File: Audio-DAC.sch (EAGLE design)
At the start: 200 parts, among them CON1 USB-5075BR-04-WH, CON2 VOL_CON, CON3 SWD_CON, IC1 3.3V 200mA, IC10 15V, IC11 -15V, IC12 3.3V, IC13 LPC1114FDH28, IC14 10V, IC15 5V, IC16 5V, IC17 3.3V, IC18 TC7WH74FU, IC19 AK4495EQ, IC2 AT32UC3A3256, IC20 TC7WU04FU, IC21 10V, IC22 -10V, IC23 OP275, IC3 SI8420, IC4 SI8420, IC5 SI8420, IC6 SI8420, IC9 7805, Q1 NPN2SC3422, Q2 PNP2SA1359, Q3 NPN2SC3422, Q4 PNP2SA1359, Q5 NPN2SC3325, Q6 NPN2SC3325, SW1 EA2, SW2 EA2, X1 12MHz, X2 24.576MHz, X3 22.5792MHz

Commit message: 微調整
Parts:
- added FB4: FB-1608, my_rcl:FB-1608
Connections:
- new net N$14: C43.1, C44.1, FB4.2, X2.VCC, X3.VCC
- new net UART_RX: IC2G$2.PX04
- new net UART_TX: IC2G$2.PX05
- net DAC_AVDD: now also FB4.1; no longer C43.1, C44.1, X2.VCC, X3.VCC
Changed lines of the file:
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@@
 <part name="SUPPLY133" library="my_supply" deviceset="DGND" device=""/>
 <part name="SUPPLY116" library="my_supply" deviceset="GND" device=""/>
+<part name="FB4" library="my_rcl" deviceset="FB" device="-1608"/>
 </parts>
 <sheets>
@@
 </segment>
 </net>
+<net name="UART_RX" class="0">
+<segment>
+<pinref part="IC2" gate="G$2" pin="PX04"/>
+<wire x1="99.06" y1="10.16" x2="93.98" y2="10.16" width="0.1524" layer="91"/>
+<label x="93.98" y="10.16" size="1.27" layer="95" rot="R180" xref="yes"/>
+</segment>
+</net>
+<net name="UART_TX" class="0">
+<segment>
+<pinref part="IC2" gate="G$2" pin="PX05"/>
+<wire x1="99.06" y1="15.24" x2="93.98" y2="15.24" width="0.1524" layer="91"/>
+<label x="93.98" y="15.24" size="1.27" layer="95" rot="R180" xref="yes"/>
+</segment>
+</net>
 </nets>
 </sheet>
@@
 </instance>
 <instance part="SUPPLY116" gate="GND" x="40.64" y="-30.48" smashed="yes"/>
+<instance part="FB4" gate="G$1" x="-58.42" y="38.1" smashed="yes" rot="R90">
+<attribute name="NAME" x="-53.34" y="36.83" size="1.778" layer="95" rot="R180"/>
+<attribute name="VALUE" x="-53.34" y="43.18" size="1.778" layer="96" rot="R180"/>
+</instance>
 </instances>
 <busses>
@@
 </segment>
 <segment>
-<pinref part="X3" gate="G$1" pin="VCC"/>
-<wire x1="-33.02" y1="17.78" x2="-35.56" y2="17.78" width="0.1524" layer="91"/>
-<pinref part="C44" gate="G$1" pin="1"/>
-<wire x1="-35.56" y1="17.78" x2="-43.18" y2="17.78" width="0.1524" layer="91"/>
-<junction x="-35.56" y="17.78"/>
-<pinref part="X2" gate="G$1" pin="VCC"/>
-<wire x1="-33.02" y1="38.1" x2="-35.56" y2="38.1" width="0.1524" layer="91"/>
-<pinref part="C43" gate="G$1" pin="1"/>
-<wire x1="-35.56" y1="38.1" x2="-43.18" y2="38.1" width="0.1524" layer="91"/>
-<junction x="-35.56" y="38.1"/>
-<wire x1="-43.18" y1="17.78" x2="-43.18" y2="38.1" width="0.1524" layer="91"/>
-<junction x="-43.18" y="38.1"/>
-<wire x1="-50.8" y1="38.1" x2="-43.18" y2="38.1" width="0.1524" layer="91"/>
-<label x="-50.8" y="38.1" size="1.778" layer="95" rot="R180" xref="yes"/>
-</segment>
-<segment>
 <pinref part="IC19" gate="G$1" pin="DEM0"/>
 <wire x1="35.56" y1="99.06" x2="38.1" y2="99.06" width="0.1524" layer="91"/>
@@
 <label x="43.18" y="96.52" size="1.27" layer="95" xref="yes"/>
 </segment>
+<segment>
+<wire x1="-68.58" y1="38.1" x2="-63.5" y2="38.1" width="0.1524" layer="91"/>
+<label x="-68.58" y="38.1" size="1.778" layer="95" rot="R180" xref="yes"/>
+<pinref part="FB4" gate="G$1" pin="1"/>
+</segment>
 </net>
 <net name="DAC_VREF" class="0">
@@
 </segment>
 </net>
+<net name="N$14" class="0">
+<segment>
+<pinref part="X3" gate="G$1" pin="VCC"/>
+<wire x1="-33.02" y1="17.78" x2="-35.56" y2="17.78" width="0.1524" layer="91"/>
+<pinref part="C44" gate="G$1" pin="1"/>
+<wire x1="-35.56" y1="17.78" x2="-43.18" y2="17.78" width="0.1524" layer="91"/>
+<junction x="-35.56" y="17.78"/>
+<pinref part="X2" gate="G$1" pin="VCC"/>
+<wire x1="-33.02" y1="38.1" x2="-35.56" y2="38.1" width="0.1524" layer="91"/>
+<pinref part="C43" gate="G$1" pin="1"/>
+<wire x1="-35.56" y1="38.1" x2="-43.18" y2="38.1" width="0.1524" layer="91"/>
+<junction x="-35.56" y="38.1"/>
+<wire x1="-43.18" y1="17.78" x2="-43.18" y2="38.1" width="0.1524" layer="91"/>
+<junction x="-43.18" y="38.1"/>
+<wire x1="-53.34" y1="38.1" x2="-43.18" y2="38.1" width="0.1524" layer="91"/>
+<pinref part="FB4" gate="G$1" pin="2"/>
+</segment>
+</net>

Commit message: 発注
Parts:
- removed JP1: SPK, pinhead:PINHD-1X4
- removed JP2: HP, pinhead:PINHD-1X4
- added R15: 100, my_rcl:R-1608J
- added R16: DNP, my_rcl:R-1608J
- added TP25: GND, my_connector:TESTPIN
- added TP26: +3V3D, my_connector:TESTPIN
- added TP27, TP31: GND_L, my_connector:TESTPIN-BIG
- added TP28: SPK_L, my_connector:TESTPIN-BIG
- added TP29: SPK_R, my_connector:TESTPIN-BIG
- added TP30, TP34: GND_R, my_connector:TESTPIN-BIG
- added TP32: HP_L, my_connector:TESTPIN-BIG
- added TP33: HP_R, my_connector:TESTPIN-BIG
- C47, C48, C52, C54: value 0.22u -> 0.1u
- C49, C50, C55, C56: value DNP -> 0.1u
- C63, C64, C65, C66: value 2000p -> 10n
- CON1: value USB-5075BR-04-WH -> USB-B; device my_connector:USB-5075BR-04-WH -> my_connector:USB-B
- CON2: value VOL_CON -> VOLUEME
- CON3: value SWD_CON -> SWD
- D7, D8: value SBD-1A -> SBD; device my_rcl:SBD-1A -> my_rcl:SBD-1A2
- FB1, FB2, FB3, FB4: value FB-1608 -> FB; device my_rcl:FB-1608 -> my_rcl:FB
- IC1: value 3.3V 200mA -> 3.3V; device my_ic:NJM2863 -> my_ic:NJM12888
- IC10: value 15V -> +15V
- IC13: value LPC1114FDH28 -> LPC1114
- IC14, IC21: value 10V -> +10V
- IC15, IC16: value 5V -> +5V
- IC17: value 3.3V -> +3.3V
- Q5, Q6: value NPN2SC3325 -> NPN
- R32, R33, R34, R35, R36: device my_rcl:R-1608 -> my_rcl:R-1608J
- R37, R38, R39, R40: value 1k -> 2k
- R41, R42, R43, R44: value 2k -> 4k
- R45, R46, R47, R48: value 1k -> 150
- TP10: value TEST_11 -> GND
- TP11: value TEST_10 -> SDA
- TP13: value GND -> TEST_10
- TP14: value +3V3 -> TEST_14
- TP15, TP18: value SP_SW -> SP
- TP16: value HP_SW -> HP
- TP17: value GND -> +12V
- TP19: value HP_SW -> GND
- TP20: value +12V -> HP
- TP23: value SDA -> TEST_11
- TP5: value VIN+ -> V+
- TP8: value VIN- -> V-
- TP9: value TEST_12 -> +3V3
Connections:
- removed net N$37: IC13.DP14, TP9.1
- removed net N$53: IC13.DP10/AN, TP11.1
- new net N$16: D7.A, Q5.C, SW1.L1
- new net N$18: IC13.DP10/AN, TP13.1
- new net N$19: IC13.DP14, TP14.1
- net +12V: now also SW1.L2, TP17.1; no longer SW1.L1, TP20.1
- net +3V3: now also TP9.1; no longer TP14.1
- net +3V3D: now also TP26.1
- net DAC_DVDD: now also IC19.DVDD; no longer IC19.DVSS
- net DAC_LRCLK: now also R15.1
- net DGND: now also TP25.1
- net EN_+3V3D: now also R16.1
- net GND: now also IC19.DVSS, TP10.1, TP19.1, TP27.1, TP30.1, TP31.1, TP34.1; no longer IC19.DVDD, JP1.1, JP1.4, JP2.1, JP2.4, TP13.1, TP17.1
- net HP_L: now also TP32.1; no longer JP2.2
- net HP_R: now also TP33.1; no longer JP2.3
- net HP_SW: now also TP20.1; no longer TP19.1
- net I2C_SDA: now also TP11.1; no longer TP23.1
- net N$36: now also IC13.DP11/AN, TP23.1; no longer D7.A, Q5.C, SW1.L2
- net N$38: now also IC13.DP2/MOSI_SPI/PWM, R15.2; no longer IC13.DP11/AN, TP10.1
- net SPK_L: now also TP28.1; no longer JP1.2
- net SPK_R: now also TP29.1; no longer JP1.3
- net USB_VBUS: now also R16.2

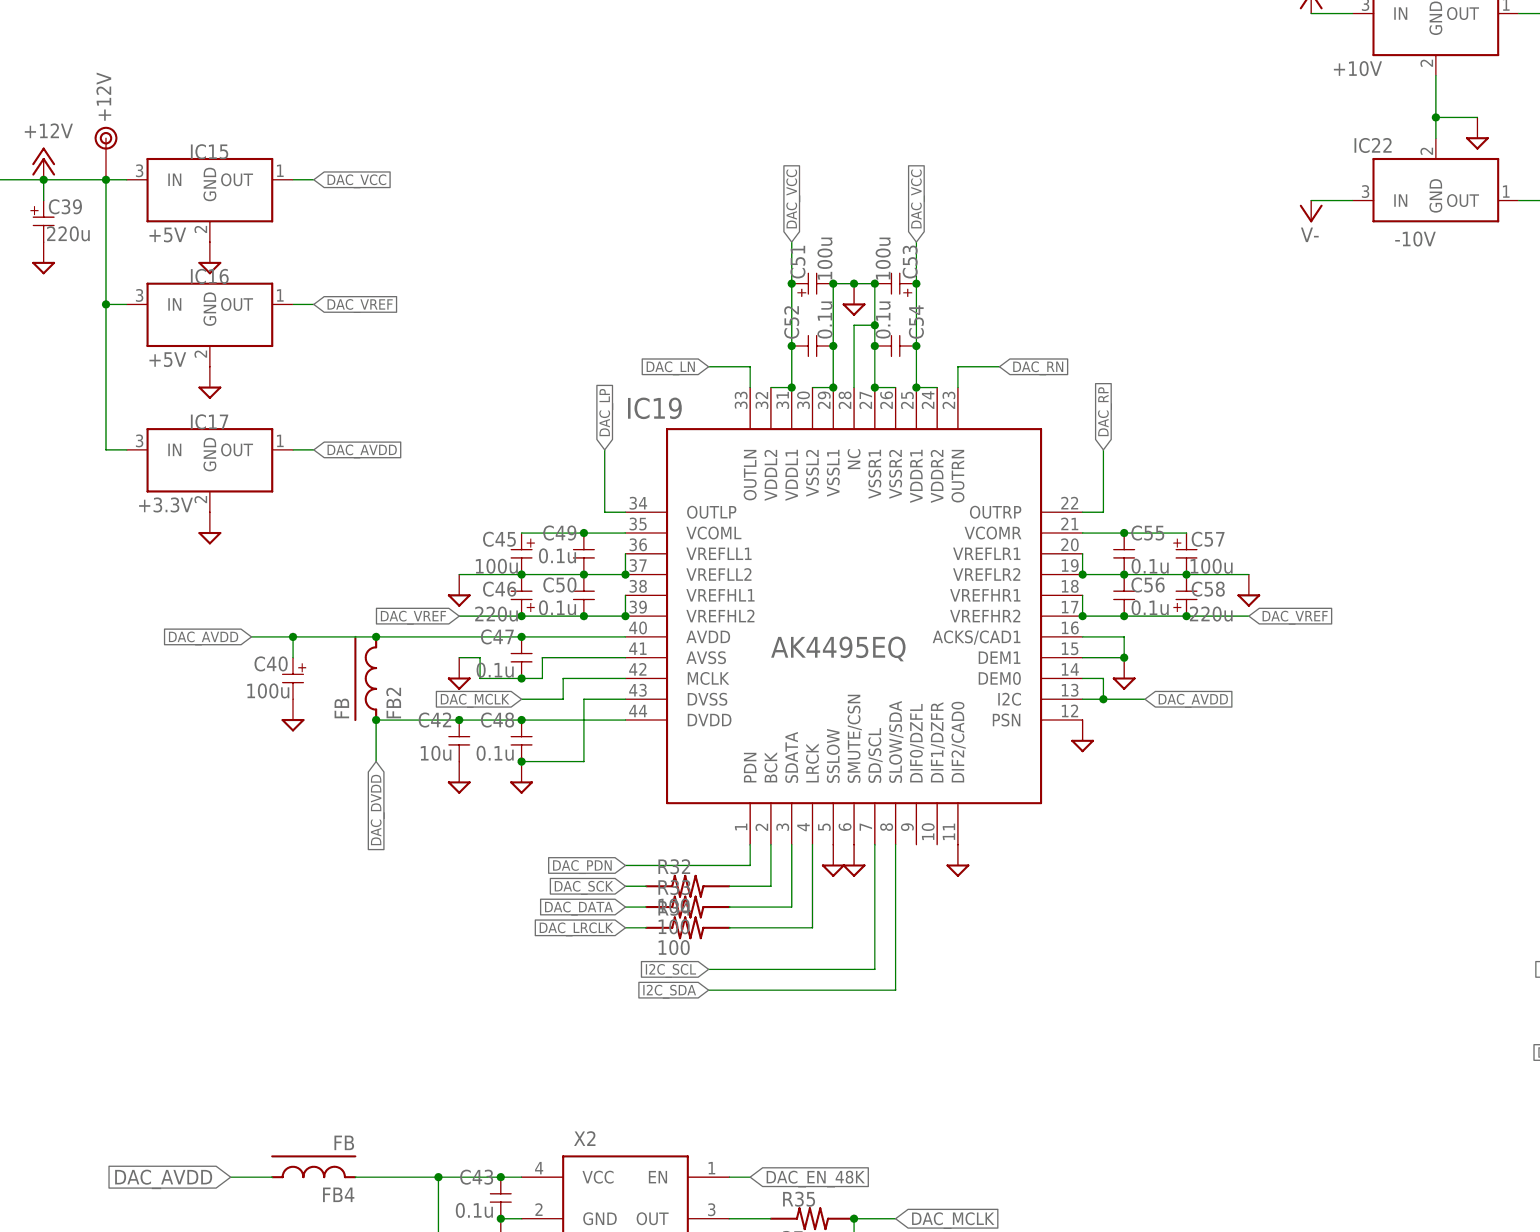
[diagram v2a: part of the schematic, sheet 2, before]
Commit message: Change to AK4493
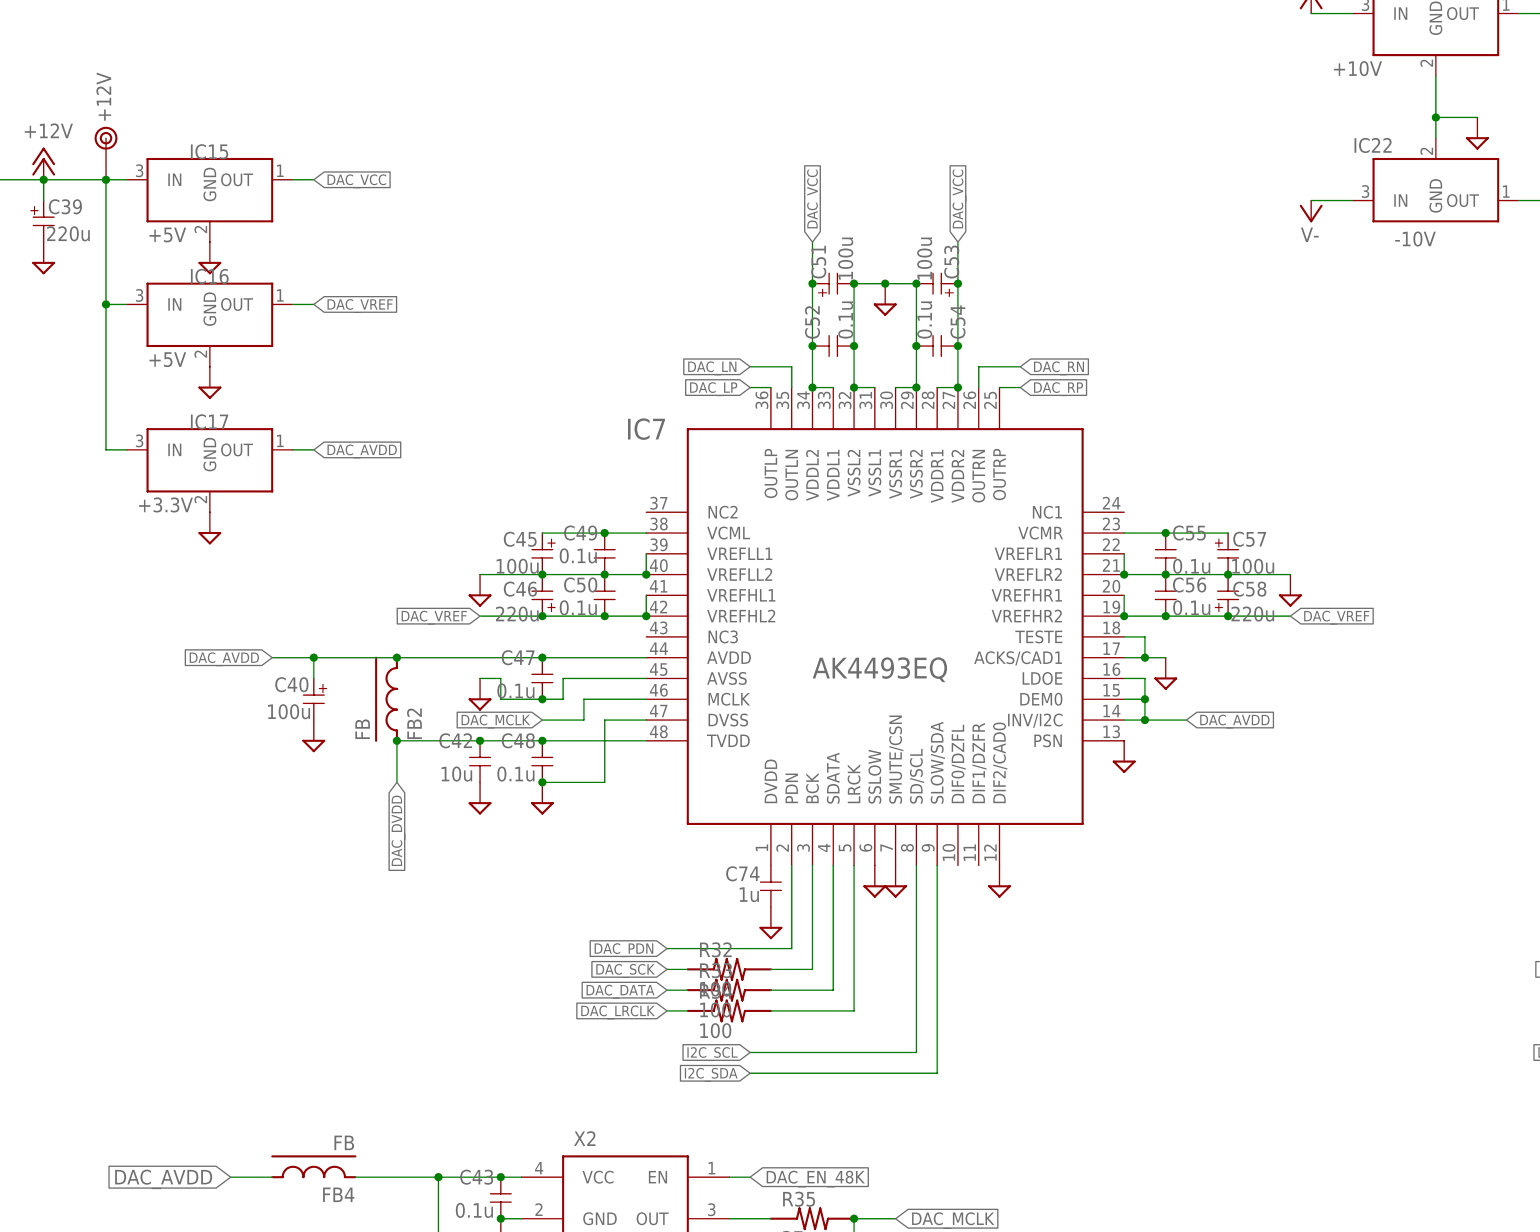
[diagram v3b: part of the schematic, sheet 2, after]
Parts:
- removed IC19: AK4495EQ, my_ic:AK4495EQ
- added C74: 1u, my_rcl:C-1608
- added IC7: AK4493EQ, my_ic:AK4493EQ
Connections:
- new net N$37: C74.1, IC7.DVDD
- net DAC_AVDD: now also IC7.AVDD, IC7.DEM0, IC7.INV/I2C, IC7.LDOE; no longer IC19.AVDD, IC19.DEM0, IC19.I2C
- net DAC_DVDD: now also IC7.TVDD; no longer IC19.DVDD
- net DAC_LN: now also IC7.OUTLN; no longer IC19.OUTLN
- net DAC_LP: now also IC7.OUTLP; no longer IC19.OUTLP
- net DAC_MCLK: now also IC7.MCLK; no longer IC19.MCLK
- net DAC_PDN: now also IC7.PDN; no longer IC19.PDN
- net DAC_RN: now also IC7.OUTRN; no longer IC19.OUTRN
- net DAC_RP: now also IC7.OUTRP; no longer IC19.OUTRP
- net DAC_VCC: now also IC7.VDDL1, IC7.VDDL2, IC7.VDDR1, IC7.VDDR2; no longer IC19.VDDL1, IC19.VDDL2, IC19.VDDR1, IC19.VDDR2
- net DAC_VREF: now also IC7.VREFHL1, IC7.VREFHL2, IC7.VREFHR1, IC7.VREFHR2; no longer IC19.VREFHL1, IC19.VREFHL2, IC19.VREFHR1, IC19.VREFHR2
- net GND: now also C74.2, IC7.ACKS/CAD1, IC7.AVSS, IC7.DIF2/CAD0, IC7.DVSS, IC7.PSN, IC7.SMUTE/CSN, IC7.SSLOW, IC7.TESTE, IC7.VREFLL1, IC7.VREFLL2, IC7.VREFLR1, IC7.VREFLR2, IC7.VSSL1, IC7.VSSL2, IC7.VSSR1, IC7.VSSR2; no longer IC19.ACKS/CAD1, IC19.AVSS, IC19.DEM1, IC19.DIF2/CAD0, IC19.DVSS, IC19.NC, IC19.PSN, IC19.SMUTE/CSN, IC19.SSLOW, IC19.VREFLL1, IC19.VREFLL2, IC19.VREFLR1, IC19.VREFLR2, IC19.VSSL1, IC19.VSSL2, IC19.VSSR1, IC19.VSSR2
- net I2C_SCL: now also IC7.SD/SCL; no longer IC19.SD/SCL
- net I2C_SDA: now also IC7.SLOW/SDA; no longer IC19.SLOW/SDA
- net N$41: now also IC7.BCK; no longer IC19.BCK
- net N$42: now also IC7.LRCK; no longer IC19.LRCK
- net N$43: now also IC7.SDATA; no longer IC19.SDATA
- net VCOM_L: now also IC7.VCML; no longer IC19.VCOML
- net VCOM_R: now also IC7.VCMR; no longer IC19.VCOMR
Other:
- moved on the sheet: C40, C42, C45, C46, C47, C48, C49, C50, C51, C52, C53, C54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

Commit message: 大体できた
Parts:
- removed C71: 10u, my_rcl:C-2012
- removed TP21: GND, my_connector:TESTPIN
- removed TP22: +12V, my_connector:TESTPIN
- TP15: value SP -> +12V
- TP16: value HP -> +12V
- TP17: value +12V -> SW_SP
- TP18: value SP -> SW_HP
- TP19: value GND -> SW_HP
- TP20: value HP -> SW_SP
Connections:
- removed net HP_SW: IC13.DP17, R59.2, TP16.1, TP20.1
- removed net N$16: D7.A, Q5.C, SW1.L1
- removed net N$49: D8.A, Q6.C, SW2.L1
- removed net SP_SW: IC13.PWM/DP18, R57.2, TP15.1, TP18.1
- new net EN_HP: IC13.DP17, R59.2
- new net EN_SP: IC13.PWM/DP18, R57.2
- new net SW_HP: D8.A, Q6.C, SW2.L1, TP18.1, TP19.1
- new net SW_SP: D7.A, Q5.C, SW1.L1, TP17.1, TP20.1
- net +12V: now also TP15.1, TP16.1; no longer C71.1, TP17.1, TP22.1
- net GND: no longer C71.2, TP19.1, TP21.1

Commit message: AK4490
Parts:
- added HT1, HT2: HEATSINK-2, my_connector:HEATSINK-2
- added Q10, Q7: NPN2SC3325, my_ic:NPN2SC3325
- added Q8, Q9: PNP2SA1313, my_ic:PNP2SA1313
- D3, D4, D5, D6: value 1N4148 -> 10m; device my_rcl:DIODE-2 -> my_rcl:CRD-SMD
- IC23: device my_ic:OPA-2' -> my_ic:OPA-2-SOP
- Q1, Q3: value NPN2SC3422 -> NPN-SOT223; device my_ic:NPN2SC3422 -> my_ic:NPN-SOT223
- Q2, Q4: value PNP2SA1359 -> PNP-SOT223; device my_ic:PNP2SA1359 -> my_ic:PNP-SOT223
- R37, R38, R39, R40, R41, R42, R43, R44, R45, R46, R47, R48: device my_rcl:R-2.5 -> my_rcl:R-1608
- R49, R50, R51, R52: value 1k -> 10k; device my_rcl:R-2.5 -> my_rcl:R-1608
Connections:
- removed net N$27: D5.K, D6.A, IC23G$2.OUT
- removed net N$60: D3.A, Q1.B, R49.1
- removed net N$64: D4.K, Q2.B, R50.2
- removed net N$75: D3.K, D4.A, IC23G$1.OUT
- new net N$16: D4.A, Q2.B, Q7.E, R50.2
- new net N$49: D3.K, Q1.B, Q8.E, R49.1
- new net N$53: IC23G$1.OUT, Q7.B, Q8.B
- new net N$54: D6.A, Q10.E, Q4.B, R52.2
- net GND: now also HT1.HT, HT2.HT
- net N$26: now also IC23G$2.OUT, Q10.B, Q9.B; no longer D5.A, Q3.B, R51.1
- net N$29: now also D5.K, Q3.B, Q9.E, R51.1; no longer D6.K, Q4.B, R52.2
- net V+: now also D3.A, D5.A, Q10.C, Q7.C
- net V-: now also D4.K, D6.K, Q8.C, Q9.C
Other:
- moved on the sheet: D7, D8, L1, L2, Q1, Q2, Q3, Q4, Q5, Q6, R49, R50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

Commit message: PCM1795途中
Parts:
- removed C57: 100u, my_rcl:CPOLE2.5-6.5
- removed C58: 220u, my_rcl:CPOLE2.5-8
- removed C74: 1u, my_rcl:C-1608
- removed FB2: FB, my_rcl:FB
- removed IC16: +5V, my_ic:78X-LED
- removed R32, R33, R34: 100, my_rcl:R-1608J
- added IC19, IC8: (no value), my_ic:OPA-2-SOP
- added R17: 10k0.1%, my_rcl:R-1608
- added R18, R19, R20, R21: (no value), my_rcl:R-1608
- C40, C45, C53: value 100u -> 0.1u; device my_rcl:CPOLE2.5-6.5 -> my_rcl:C-1608
- C42: value 10u -> 0.1u; device my_rcl:C-2012 -> my_rcl:C-1608
- C46: value 220u -> 0.1u; device my_rcl:CPOLE2.5-8 -> my_rcl:C-1608
- C47, C48, C54, C55: value 0.1u -> 100u; device my_rcl:C-1608 -> my_rcl:CPOLE2.5-6.5
- C49, C50, C52: value 0.1u -> (none)
- C51: value 100u -> (none); device my_rcl:CPOLE2.5-6.5 -> my_rcl:C-1608
- C56: value 0.1u -> 10u; device my_rcl:C-1608 -> my_rcl:C-2012
- IC7: value AK4493EQ -> PCM1795; device my_ic:AK4493EQ -> my_ic:PCM1795
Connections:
- removed net DAC_AVDD: C40.1, C47.1, FB2.1, FB4.1, IC17.OUT, IC7.AVDD, IC7.DEM0, IC7.INV/I2C, IC7.LDOE
- removed net DAC_DVDD: C42.1, C48.1, FB2.2, IC7.TVDD
- removed net DAC_VREF: C46.1, C50.2, C56.2, C58.1, IC16.OUT, IC7.VREFHL1, IC7.VREFHL2, IC7.VREFHR1, IC7.VREFHR2
- removed net N$14: C43.1, C44.1, FB4.2, X2.VCC, X3.VCC
- removed net N$41: IC7.BCK, R32.2
- removed net N$42: IC7.LRCK, R34.2
- removed net N$43: IC7.SDATA, R33.2
- removed net VCOM_L: C45.1, C49.1, IC7.VCML
- removed net VCOM_R: C55.1, C57.1, IC7.VCMR
- new net CLK_VDD: C43.1, C44.1, C56.1, FB4.2, X2.VCC, X3.VCC
- new net DAC_VDD: C53.1, C54.1, FB4.1, IC17.OUT, IC7.MSEL, IC7.VDD
- new net IOUTL+: C49.1, IC7.IOUTL+, IC8G$1.-IN, R18.1
- new net IOUTL-: C50.1, C52.1, IC19G$2.-IN, IC7.IOUTL-, IC8G$2.-IN, R19.1, R21.1
- new net IOUTR+: C51.1, IC19G$1.-IN, IC7.IOUTR+, R20.1
- new net IOUTR-: IC7.IOUTR-
- new net N$27: IC7.IREF, R17.2
- net +12V: no longer IC16.IN
- net DAC_DATA: now also IC5.OUT2, IC7.DATA; no longer IC5.OUT1, R33.1
- net DAC_EN_48K: now also IC4.OUT2
- net DAC_EN_48K_IN: no longer IC4.OUT1
- net DAC_LN: now also C50.2, IC8G$2.OUT, R19.2; no longer IC7.OUTLN
- net DAC_LP: now also C49.2, IC8G$1.OUT, R18.2; no longer IC7.OUTLP
- net DAC_LRCLK: now also IC5.OUT1, IC7.LRCK; no longer IC5.OUT2, R34.1
- net DAC_MCLK: now also IC3.IN2, IC7.SCK; no longer IC7.MCLK
- net DAC_MCLK/2: no longer IC3.IN1
- net DAC_PDN: no longer IC7.PDN
- net DAC_RN: now also C52.2, IC19G$2.OUT, R21.2; no longer IC7.OUTRN
- net DAC_RP: now also C51.2, IC19G$1.OUT, R20.2; no longer IC7.OUTRP
- net DAC_SCK: now also IC4.OUT1, IC7.BCK; no longer IC4.OUT2, R32.1
- net DAC_VCC: now also C40.1, C42.1, C45.1, C46.1, C47.1, C48.1, C55.1, IC7.VCC1, IC7.VCC2L, IC7.VCC2R; no longer C51.1, C52.1, C53.1, C54.1, IC7.VDDL1, IC7.VDDL2, IC7.VDDR1, IC7.VDDR2
- net D_DATA: now also IC5.IN2; no longer IC5.IN1
- net D_EN_48K: now also IC4.IN2; no longer IC4.IN1
- net D_LRCLK: now also IC5.IN1; no longer IC5.IN2
- net D_SCK: now also IC4.IN1; no longer IC4.IN2
- net GND: now also C56.2, IC19G$1.+IN, IC19G$2.+IN, IC3.IN1, IC7.!MS, IC7.AGND1, IC7.AGND2, IC7.AGND3L, IC7.AGND3R, IC7.DGND, IC7.MDI, IC8G$1.+IN, IC8G$2.+IN, R17.1; no longer C46.2, C47.2, C49.2, C50.1, C51.2, C52.2, C56.1, C57.2, C58.2, C74.2, IC16.GND, IC3.IN2, IC7.ACKS/CAD1, IC7.AVSS, IC7.DIF2/CAD0, IC7.DVSS, IC7.PSN, IC7.SMUTE/CSN, IC7.SSLOW, IC7.TESTE, IC7.VREFLL1, IC7.VREFLL2, IC7.VREFLR1, IC7.VREFLR2, IC7.VSSL1, IC7.VSSL2, IC7.VSSR1, IC7.VSSR2
- net I2C_SCL: now also IC7.MC; no longer IC7.SD/SCL
- net I2C_SDA: now also IC7.MDO; no longer IC7.SLOW/SDA
- net N$37: now also C46.2, C47.2, IC7.VCOML, IC7.VCOMR; no longer C74.1, IC7.DVDD
- net OPA_+: now also IC19G$3.V+, IC8G$3.V+
- net OPA_-: now also IC19G$3.V-, IC8G$3.V-
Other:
- moved on the sheet: C42, C49, C50, C52, C56, C63, C64, C65, C66, C67, C68, C69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
